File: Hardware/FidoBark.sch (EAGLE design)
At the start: 37 parts, among them T1 BPX81, U3 HM-10

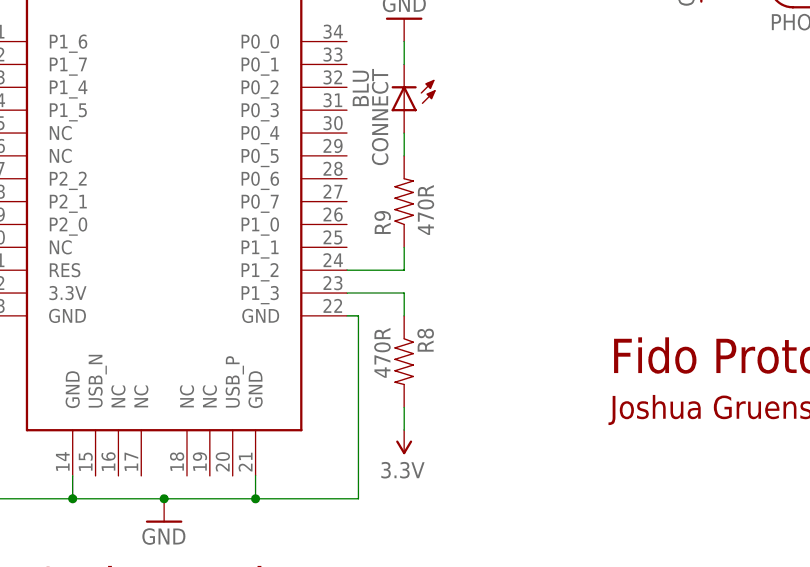
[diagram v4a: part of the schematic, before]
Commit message: piezo and led
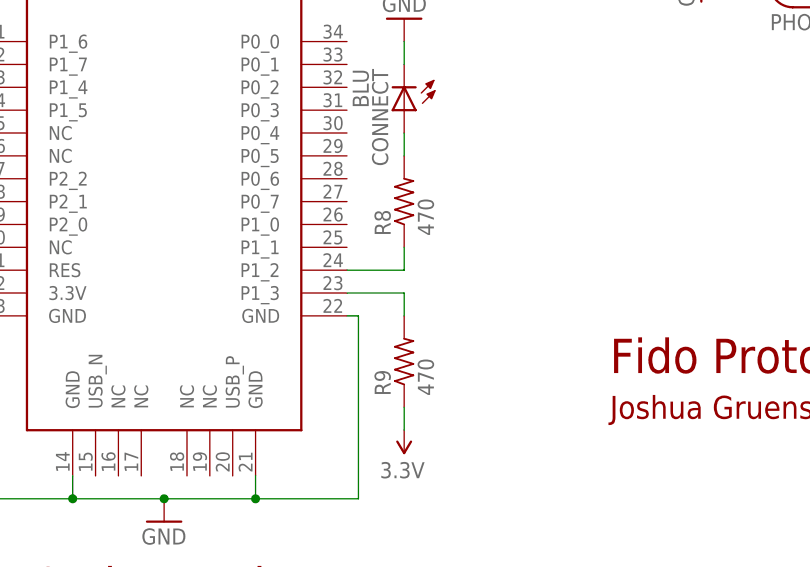
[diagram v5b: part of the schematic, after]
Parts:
- R8, R9: value 470R -> 470; device SparkFun-Resistors:0.3OHM-1/8W-1%(0805) -> adafruit:R-US_R0603
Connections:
- net 3.3V: now also R9.1; no longer R8.2
- net N$10: now also R8.1; no longer R9.1
- net N$11: now also R9.2; no longer R8.1
- net N$16: now also R8.2; no longer R9.2
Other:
- moved on the sheet: R8, R9
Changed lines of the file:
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@@
 <setting verticaltext="up"/>
 </settings>
-<grid distance="0.1" unitdist="inch" unit="inch" style="lines" multiple="1" display="no" altdistance="0.01" altunitdist="inch" altunit="inch"/>
+<grid distance="0.1" unitdist="inch" unit="inch" style="lines" multiple="1" display="no" altdistance="0.05" altunitdist="inch" altunit="inch"/>
 <layers>
 <layer number="1" name="Top" color="4" fill="1" visible="no" active="no"/>
@@
 <part name="GND11" library="SparkFun-Aesthetics" deviceset="GND" device=""/>
 <part name="U3" library="HM-10_BLE" deviceset="HM-10" device=""/>
-<part name="R8" library="SparkFun-Resistors" deviceset="0.3OHM-1/8W-1%(0805)" device="" value="470R"/>
-<part name="R9" library="SparkFun-Resistors" deviceset="0.3OHM-1/8W-1%(0805)" device="" value="470R"/>
 <part name="CONNECT" library="adafruit" deviceset="LED" device="CHIPLED_0805" value="BLU"/>
 <part name="GND17" library="supply1" deviceset="GND" device=""/>
@@
 <part name="GND12" library="supply1" deviceset="GND" device=""/>
 <part name="J1" library="SparkFun-Connectors" deviceset="JST_2MM_MALE" device=""/>
+<part name="R8" library="adafruit" deviceset="R-US_" device="R0603" value="470"/>
+<part name="R9" library="adafruit" deviceset="R-US_" device="R0603" value="470"/>
 </parts>
 <sheets>
@@
 <instance part="GND11" gate="1" x="154.94" y="55.88" rot="R90"/>
 <instance part="U3" gate="G$1" x="36.83" y="44.45"/>
-<instance part="R8" gate="G$1" x="63.5" y="31.75" rot="R270"/>
-<instance part="R9" gate="G$1" x="63.5" y="49.53" rot="R90"/>
 <instance part="CONNECT" gate="G$1" x="63.5" y="59.69" rot="R180"/>
 <instance part="GND17" gate="1" x="36.83" y="13.97"/>
@@
 <instance part="GND12" gate="1" x="175.26" y="154.94"/>
 <instance part="J1" gate="G$1" x="167.64" y="160.02" rot="R90"/>
+<instance part="R8" gate="G$1" x="63.5" y="49.53" rot="R90"/>
+<instance part="R9" gate="G$1" x="63.5" y="31.75" rot="R90"/>
 </instances>
 <busses>
@@
 </segment>
 <segment>
-<pinref part="R8" gate="G$1" pin="2"/>
 <pinref part="SUPPLY11" gate="G$1" pin="3.3V"/>
 <wire x1="63.5" y1="24.13" x2="63.5" y2="26.67" width="0.1524" layer="91"/>
+<pinref part="R9" gate="G$1" pin="1"/>
 </segment>
 <segment>
@@
 <net name="N$16" class="0">
 <segment>
-<pinref part="R9" gate="G$1" pin="2"/>
 <pinref part="CONNECT" gate="G$1" pin="A"/>
 <wire x1="63.5" y1="54.61" x2="63.5" y2="57.15" width="0.1524" layer="91"/>
+<pinref part="R8" gate="G$1" pin="2"/>
 </segment>
 </net>
@@
 <net name="N$10" class="0">
 <segment>
-<pinref part="R9" gate="G$1" pin="1"/>
 <wire x1="63.5" y1="44.45" x2="63.5" y2="41.91" width="0.1524" layer="91"/>
 <pinref part="U3" gate="G$1" pin="P1_2"/>
 <wire x1="63.5" y1="41.91" x2="57.15" y2="41.91" width="0.1524" layer="91"/>
+<pinref part="R8" gate="G$1" pin="1"/>
 </segment>
 </net>
@@
 <pinref part="U3" gate="G$1" pin="P1_3"/>
 <wire x1="57.15" y1="39.37" x2="63.5" y2="39.37" width="0.1524" layer="91"/>
-<pinref part="R8" gate="G$1" pin="1"/>
 <wire x1="63.5" y1="39.37" x2="63.5" y2="36.83" width="0.1524" layer="91"/>
-</segment>
-</net>
+<pinref part="R9" gate="G$1" pin="2"/>
+</segment>
+</net>

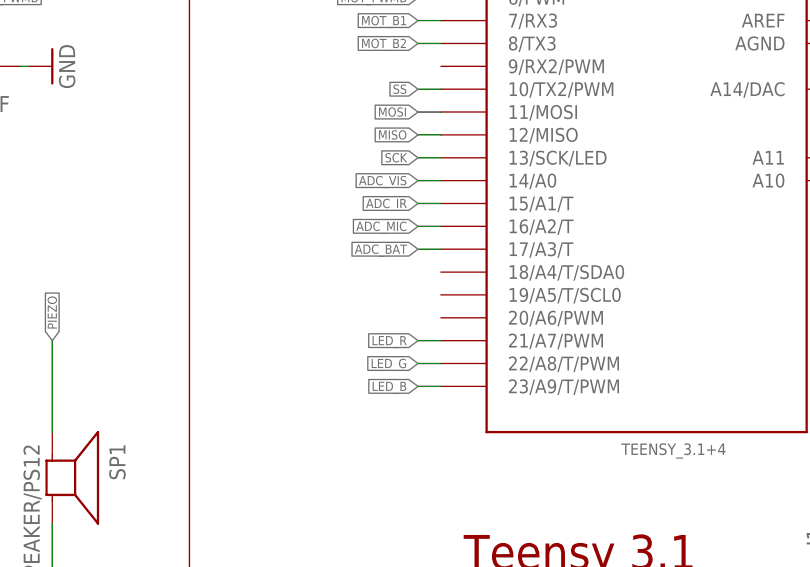
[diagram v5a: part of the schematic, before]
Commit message: forgot teensy i2c
oops
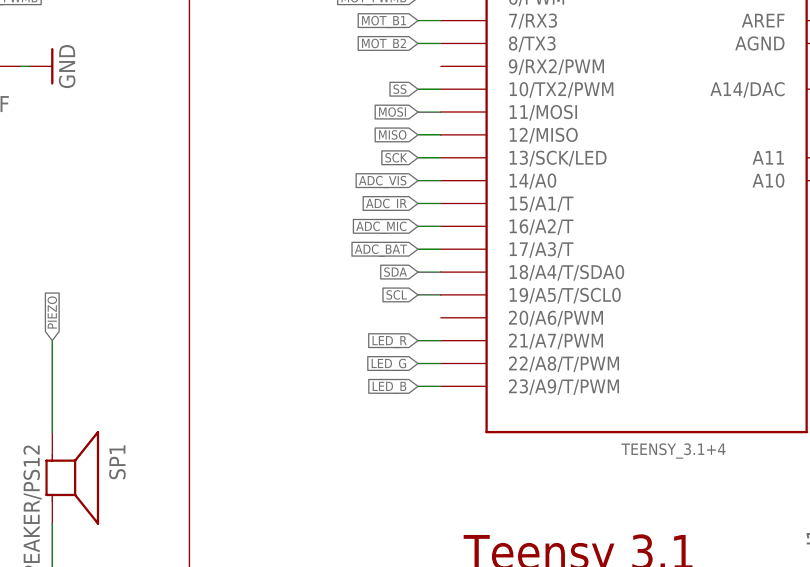
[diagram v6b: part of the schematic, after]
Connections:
- net SCL: now also U$1.19/A5/T/SCL0
- net SDA: now also U$1.18/A4/T/SDA0
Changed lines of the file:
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@@
 <label x="68.58" y="111.76" size="1.016" layer="95" xref="yes"/>
+</segment>
+<segment>
+<pinref part="U$1" gate="G$1" pin="18/A4/T/SDA0"/>
+<wire x1="119.38" y1="187.96" x2="116.84" y2="187.96" width="0.1524" layer="91"/>
+<label x="116.84" y="187.96" size="1.016" layer="95" rot="R180" xref="yes"/>
 </segment>
 </net>
@@
 <label x="68.58" y="109.22" size="1.016" layer="95" xref="yes"/>
 </segment>
+<segment>
+<pinref part="U$1" gate="G$1" pin="19/A5/T/SCL0"/>
+<wire x1="119.38" y1="185.42" x2="116.84" y2="185.42" width="0.1524" layer="91"/>
+<label x="116.84" y="185.42" size="1.016" layer="95" rot="R180" xref="yes"/>
+</segment>
 </net>

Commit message: fucking finished it
goddamn
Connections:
- net GND: now also U$5.2; no longer U$5.1
- net N$28: now also U$5.1; no longer U$5.2
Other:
- moved on the sheet: U$5
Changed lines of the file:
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@@
 <instance part="GND21" gate="1" x="96.52" y="73.66" rot="R270"/>
 <instance part="SUPPLY20" gate="G$1" x="119.38" y="88.9"/>
-<instance part="U$5" gate="G$1" x="106.68" y="111.76" rot="R90"/>
+<instance part="U$5" gate="G$1" x="106.68" y="114.3" rot="MR270"/>
 <instance part="GND28" gate="1" x="149.86" y="99.06"/>
 <instance part="GND34" gate="1" x="137.16" y="88.9"/>
@@
 </segment>
 <segment>
-<pinref part="U$5" gate="G$1" pin="1"/>
 <pinref part="GND35" gate="1" pin="GND"/>
+<wire x1="111.76" y1="111.76" x2="111.76" y2="109.22" width="0.1524" layer="91"/>
+<pinref part="U$5" gate="G$1" pin="2"/>
 <wire x1="109.22" y1="111.76" x2="111.76" y2="111.76" width="0.1524" layer="91"/>
-<wire x1="111.76" y1="111.76" x2="111.76" y2="109.22" width="0.1524" layer="91"/>
 </segment>
 <segment>
@@
 <net name="N$28" class="0">
 <segment>
-<pinref part="U$5" gate="G$1" pin="2"/>
 <pinref part="C13" gate="G$1" pin="1"/>
-<wire x1="109.22" y1="114.3" x2="111.76" y2="114.3" width="0.1524" layer="91"/>
 <pinref part="R14" gate="G$1" pin="1"/>
 <wire x1="111.76" y1="114.3" x2="114.3" y2="114.3" width="0.1524" layer="91"/>
 <wire x1="111.76" y1="114.3" x2="111.76" y2="116.84" width="0.1524" layer="91"/>
+<pinref part="U$5" gate="G$1" pin="1"/>
+<wire x1="111.76" y1="114.3" x2="109.22" y2="114.3" width="0.1524" layer="91"/>
 <junction x="111.76" y="114.3"/>
 </segment>

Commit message: prep for gerber export
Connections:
- removed net VUSB: U$1.VUSB
- net V_BATT: now also U$1.VIN
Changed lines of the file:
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@@
 <setting verticaltext="up"/>
 </settings>
-<grid distance="0.1" unitdist="inch" unit="inch" style="lines" multiple="1" display="no" altdistance="0.05" altunitdist="inch" altunit="inch"/>
+<grid distance="0.1" unitdist="inch" unit="inch" style="lines" multiple="1" display="no" altdistance="0.01" altunitdist="inch" altunit="inch"/>
 <layers>
 <layer number="1" name="Top" color="4" fill="1" visible="no" active="no"/>
@@
 <part name="R8" library="adafruit" deviceset="R-US_" device="R0603" value="470"/>
 <part name="R9" library="adafruit" deviceset="R-US_" device="R0603" value="470"/>
+<part name="SUPPLY10" library="SparkFun-Aesthetics" deviceset="V_BATT" device=""/>
 </parts>
 <sheets>
@@
 <instance part="FRAME1" gate="G$2" x="83.82" y="0"/>
 <instance part="SUPPLY1" gate="G$1" x="170.18" y="231.14" smashed="yes" rot="R270">
-<attribute name="VALUE" x="168.656" y="232.156" size="1.778" layer="96"/>
+<attribute name="VALUE" x="167.386" y="228.092" size="1.778" layer="96"/>
 </instance>
 <instance part="GND1" gate="1" x="172.72" y="220.98"/>
@@
 <instance part="R8" gate="G$1" x="63.5" y="49.53" rot="R90"/>
 <instance part="R9" gate="G$1" x="63.5" y="31.75" rot="R90"/>
+<instance part="SUPPLY10" gate="G$1" x="170.18" y="233.68" smashed="yes" rot="R270">
+<attribute name="VALUE" x="166.116" y="234.696" size="1.778" layer="96"/>
+</instance>
 </instances>
 <busses>
 </busses>
 <nets>
-<net name="VUSB" class="0">
-<segment>
-<pinref part="U$1" gate="G$1" pin="VUSB"/>
-<wire x1="165.1" y1="236.22" x2="167.64" y2="236.22" width="0.1524" layer="91"/>
-<label x="167.64" y="236.22" size="1.016" layer="95" xref="yes"/>
-</segment>
-</net>
 <net name="3.3V" class="0">
 <segment>
@@
 <wire x1="175.26" y1="162.56" x2="172.72" y2="162.56" width="0.1524" layer="91"/>
 </segment>
-</net>
+<segment>
+<pinref part="SUPPLY10" gate="G$1" pin="V_BATT"/>
+<pinref part="U$1" gate="G$1" pin="VIN"/>
+<wire x1="170.18" y1="233.68" x2="165.1" y2="233.68" width="0.1524" layer="91"/>
+</segment>
+</net>
